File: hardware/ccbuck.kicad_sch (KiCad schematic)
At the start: 38 parts, among them J3 PWM/PFM, Q20 2N7002, U17 TPS552872RYQR

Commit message: craigenyah
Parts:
- renumbered C103 to C10, C104 to C11, C105 to C12, C106 to C13, C107 to C14, C88 to C15, C102 to C16, C124 to C17, C99 to C18, C100 to C19, C92 to C20, C91 to C21, C89 to C22, C90 to C23, C101 to C9, D10 to D9, J3 to J4, L2 to L1, Q20 to Q7, R126 to R18, R127 to R19, R125 to R20, R137 to R21, R138 to R22, R115 to R23, R114 to R24, R139 to R25, R41 to R26, R42 to R27, R132 to R28, R130 to R29, R131 to R30, TP35 to TP5, TP53 to TP6, TP51 to TP7, TP52 to TP8, U17 to U1

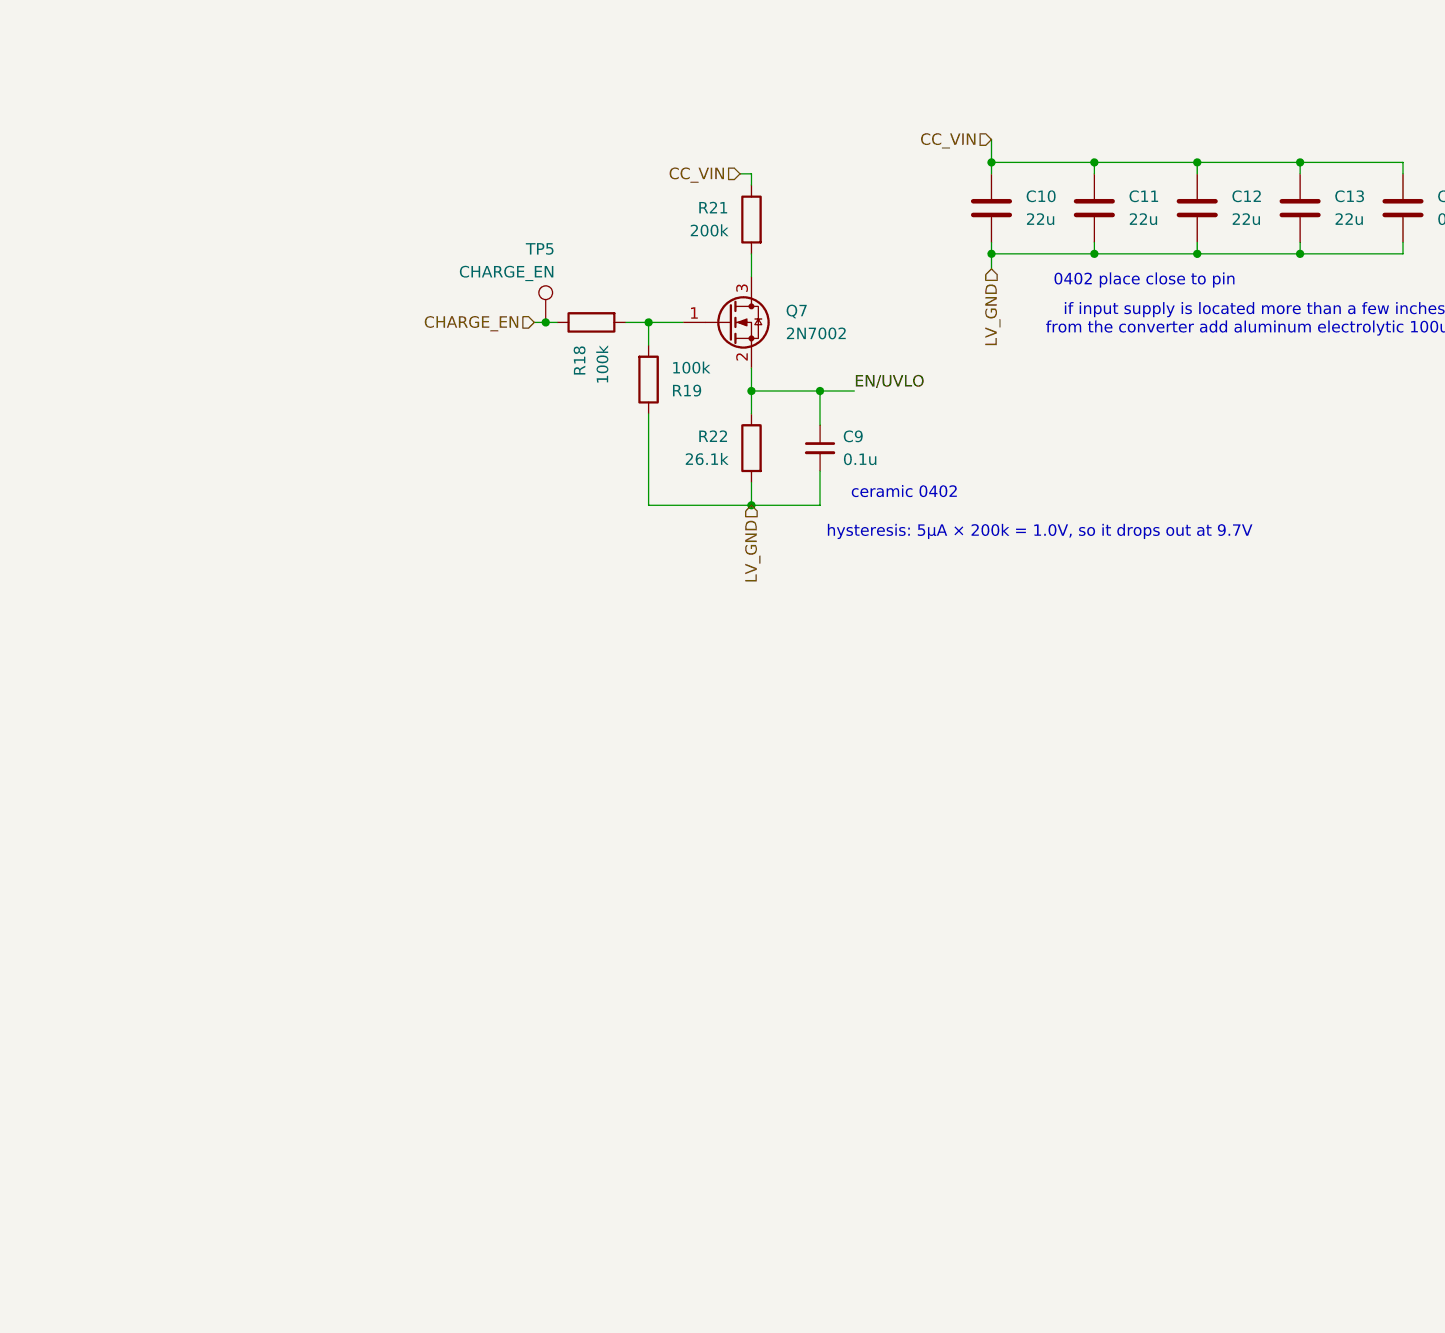
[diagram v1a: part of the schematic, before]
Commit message: switch to laptop
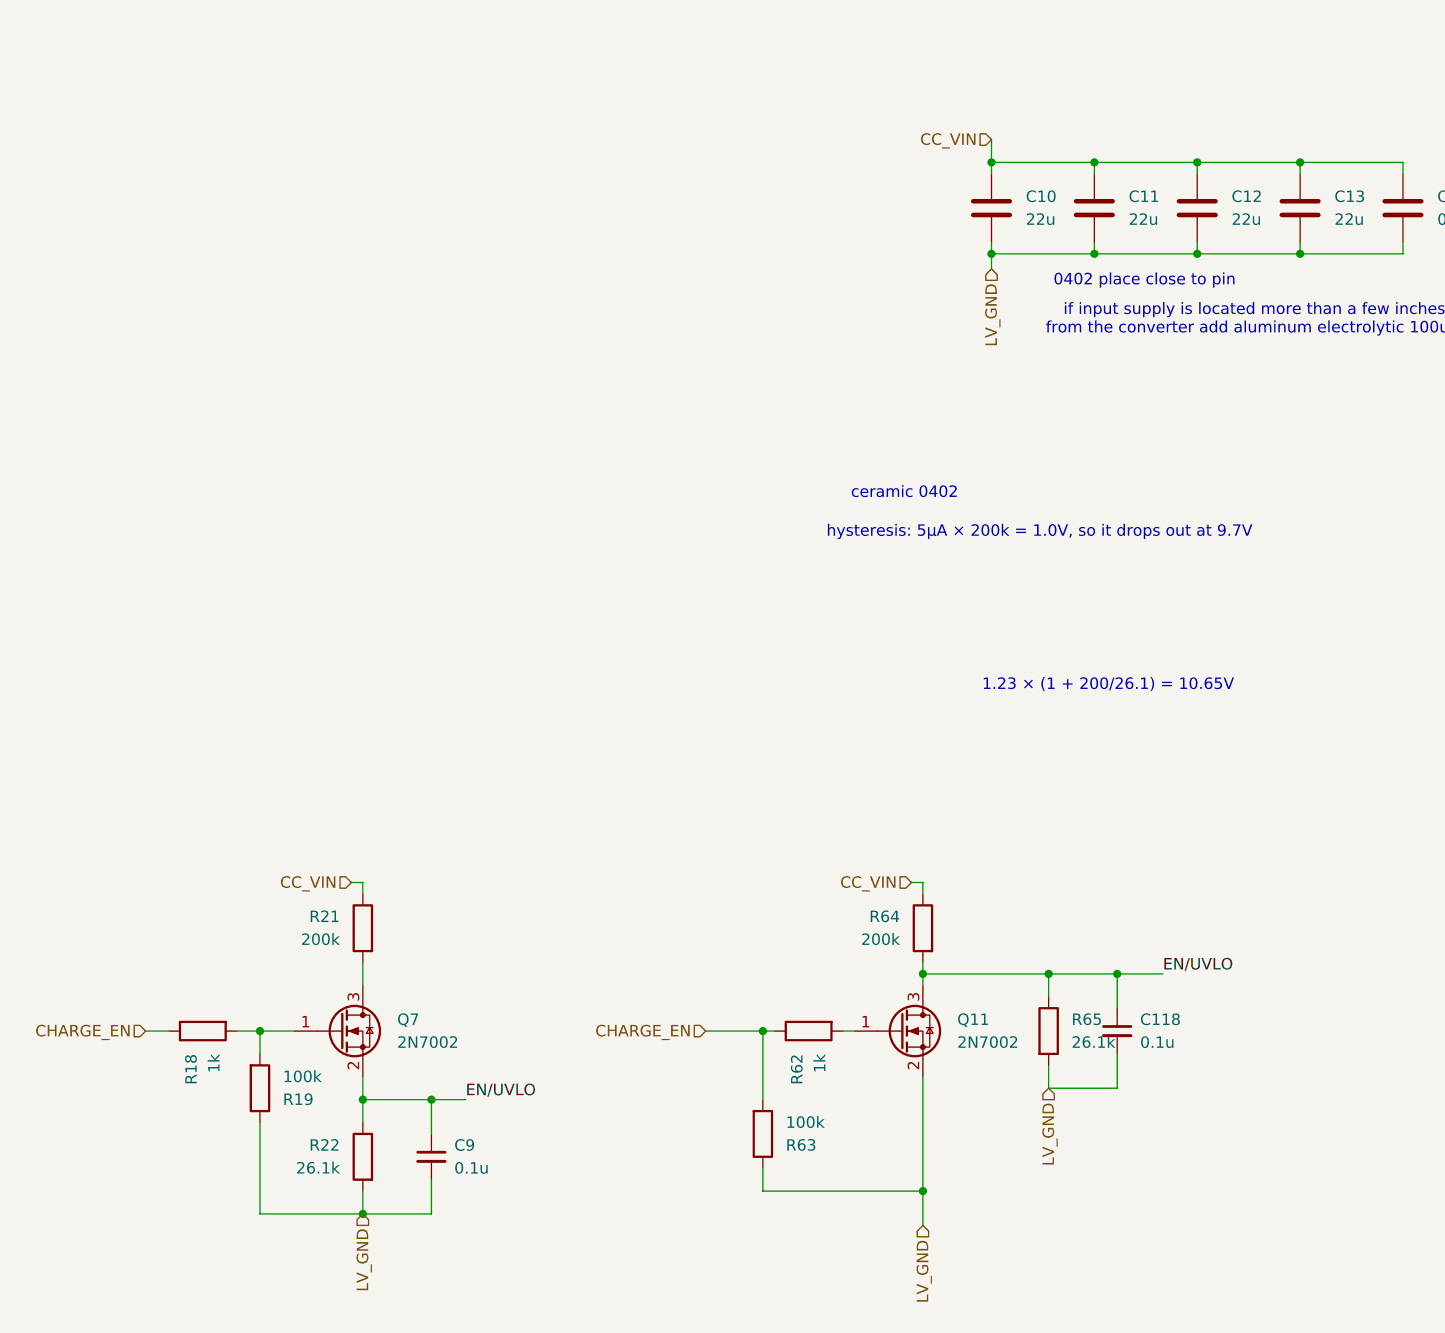
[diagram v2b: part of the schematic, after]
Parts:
- removed TP5: CHARGE_EN, TestPoint:TestPoint_Loop_D2.50mm_Drill1.0mm_LowProfile, symbol Connector:TestPoint
- added C118: 0.1u, Capacitor_SMD:C_0402_1005Metric_Pad0.74x0.62mm_HandSolder, symbol Device:C_Small
- added Q11: 2N7002, Package_TO_SOT_SMD:SOT-23, symbol Transistor_FET:2N7002
- added R62: 1k, Resistor_SMD:R_0603_1608Metric_Pad0.98x0.95mm_HandSolder, symbol Device:R
- added R63: 100k, Resistor_SMD:R_0603_1608Metric_Pad0.98x0.95mm_HandSolder, symbol Device:R
- added R64: 200k, Resistor_SMD:R_0603_1608Metric_Pad0.98x0.95mm_HandSolder, symbol Device:R
- added R65: 26.1k, Resistor_SMD:R_0603_1608Metric_Pad0.98x0.95mm_HandSolder, symbol Device:R
- R18: value 100k -> 1k
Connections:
- net CC_VIN: now also R64.1
- net CHARGE_EN: now also R62.1, R63.2
- net EN/UVLO: now also C118.1, Q11.3 (D), R64.2, R65.1
- net LV_GND: now also C118.2, Q11.2 (S), R63.1, R65.2
- new net: Q11.1 (G), R62.2
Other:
- note added: "1.23 × (1 + 200/26.1) = 10.65V"
- moved on the sheet: C9, Q7, R18, R19, R21, R22

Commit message: switch back to pc
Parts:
- removed C9: 0.1u, Capacitor_SMD:C_0402_1005Metric_Pad0.74x0.62mm_HandSolder, symbol Device:C_Small
- removed Q7: 2N7002, Package_TO_SOT_SMD:SOT-23, symbol Transistor_FET:2N7002
- removed R18: 1k, Resistor_SMD:R_0603_1608Metric_Pad0.98x0.95mm_HandSolder, symbol Device:R
- removed R19: 100k, Resistor_SMD:R_0603_1608Metric_Pad0.98x0.95mm_HandSolder, symbol Device:R
- removed R21: 200k, Resistor_SMD:R_0603_1608Metric_Pad0.98x0.95mm_HandSolder, symbol Device:R
- removed R22: 26.1k, Resistor_SMD:R_0603_1608Metric_Pad0.98x0.95mm_HandSolder, symbol Device:R
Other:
- moved on the sheet: C10, C11, C118, C12, C13, C14, Q11, R62, R63, R64, R65

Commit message: switch to pc...
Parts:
- R28: symbol Device:R_Shunt -> Device:R
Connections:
- net AGND is gone; now on net LV_GND: U1.17 (AGND)
- net SW1 is gone; now on net LV_GND: C18.2, L1.1, TP7.1, U1.8 (SW1)
- net CC_VOUT: now also U1.13 (ISN)
- net ISP: now also C20.1, C21.1, C22.1, C23.1, R28.2, U1.11 (VOUT); no longer R28.3
- removed net ISN: R28.2, U1.13 (ISN)
- removed net VOUT: C20.1, C21.1, C22.1, C23.1, R28.4, U1.11 (VOUT)
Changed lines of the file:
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@@
+	)
+	(junction
+		(at 187.96 109.22)
+		(diameter 0)
+		(color 0 0 0 0)
 	)
 	(junction
@@
 	)
 	(junction
+		(at 175.26 109.22)
+		(diameter 0)
+		(color 0 0 0 0)
+	)
+	(junction
 		(at 201.93 87.63)
 		(diameter 0)
@@
 	(wire
 		(pts
-			(xy 186.69 111.76) (xy 186.69 116.84)
-		)
-		(stroke
-			(width 0)
-			(type default)
-		)
-	)
-	(wire
-		(pts
 			(xy 81.28 161.29) (xy 81.28 157.48)
 		)
@@
 	(wire
 		(pts
+			(xy 187.96 109.22) (xy 198.12 109.22)
+		)
+		(stroke
+			(width 0)
+			(type default)
+		)
+	)
+	(wire
+		(pts
 			(xy 57.15 172.72) (xy 57.15 176.53)
 		)
@@
 	(wire
 		(pts
-			(xy 107.95 101.6) (xy 118.11 101.6)
-		)
-		(stroke
-			(width 0)
-			(type default)
-		)
-	)
-	(wire
-		(pts
 			(xy 238.76 128.27) (xy 248.92 128.27)
 		)
@@
 	(wire
 		(pts
-			(xy 175.26 104.14) (xy 166.37 104.14)
+			(xy 166.37 104.14) (xy 187.96 104.14)
 		)
 		(stroke
@@
 	(wire
 		(pts
-			(xy 189.23 109.22) (xy 198.12 109.22)
-		)
-		(stroke
-			(width 0)
-			(type default)
-		)
-	)
-	(wire
-		(pts
 			(xy 175.26 106.68) (xy 166.37 106.68)
 		)
@@
 	(wire
 		(pts
+			(xy 175.26 109.22) (xy 177.8 109.22)
+		)
+		(stroke
+			(width 0)
+			(type default)
+		)
+	)
+	(wire
+		(pts
 			(xy 107.95 86.36) (xy 118.11 86.36)
 		)
@@
 	(wire
 		(pts
+			(xy 185.42 109.22) (xy 187.96 109.22)
+		)
+		(stroke
+			(width 0)
+			(type default)
+		)
+	)
+	(wire
+		(pts
 			(xy 53.34 87.63) (xy 59.69 87.63)
 		)
@@
 	(wire
 		(pts
+			(xy 105.41 101.6) (xy 118.11 101.6)
+		)
+		(stroke
+			(width 0)
+			(type default)
+		)
+	)
+	(wire
+		(pts
 			(xy 90.17 120.65) (xy 78.74 120.65)
 		)
@@
 	(wire
 		(pts
-			(xy 175.26 93.98) (xy 166.37 93.98)
+			(xy 166.37 93.98) (xy 177.8 93.98)
 		)
 		(stroke
@@
 	(wire
 		(pts
+			(xy 187.96 104.14) (xy 187.96 109.22)
+		)
+		(stroke
+			(width 0)
+			(type default)
+		)
+	)
+	(wire
+		(pts
 			(xy 238.76 137.16) (xy 238.76 138.43)
 		)
@@
 	(wire
 		(pts
+			(xy 175.26 106.68) (xy 175.26 109.22)
+		)
+		(stroke
+			(width 0)
+			(type default)
+		)
+	)
+	(wire
+		(pts
 			(xy 198.12 133.35) (xy 198.12 132.08)
 		)
@@
 	(wire
 		(pts
-			(xy 181.61 111.76) (xy 181.61 116.84)
-		)
-		(stroke
-			(width 0)
-			(type default)
-		)
-	)
-	(wire
-		(pts
 			(xy 156.21 130.81) (xy 161.29 130.81)
 		)
@@
 	(wire
 		(pts
-			(xy 166.37 109.22) (xy 179.07 109.22)
+			(xy 166.37 109.22) (xy 175.26 109.22)
 		)
 		(stroke
@@
 		)
 	)
-	(label "ISN"
-		(at 186.69 116.84 180)
-		(effects
-			(font
-				(size 1.27 1.27)
-			)
-			(justify right bottom)
-		)
-	)
 	(label "FSW"
 		(at 57.15 43.18 180)
@@
 			)
 			(justify left bottom)
-		)
-	)
-	(label "ISP"
-		(at 181.61 116.84 180)
-		(effects
-			(font
-				(size 1.27 1.27)
-			)
-			(justify right bottom)
 		)
 	)
@@
 		(shape input)
 		(at 198.12 133.35 270)
+		(effects
+			(font
+				(size 1.27 1.27)
+			)
+			(justify right)
+		)
+	)
+	(hierarchical_label "LV_GND"
+		(shape input)
+		(at 177.8 93.98 270)
+		(effects
+			(font
+				(size 1.27 1.27)
+			)
+			(justify right)
+		)
+	)
+	(hierarchical_label "LV_GND"
+		(shape input)
+		(at 105.41 101.6 270)
 		(effects
 			(font
@@
 	)
 	(symbol
-		(lib_id "Device:R_Shunt")
-		(at 184.15 109.22 270)
+		(lib_id "Device:R")
+		(at 181.61 109.22 270)
 		(unit 1)
 		(body_style 1)
@@
 		(dnp no)
 		(property "Reference" "R28"
-			(at 184.15 102.87 90)
+			(at 181.61 102.87 90)
 			(show_name no)
 			(do_not_autoplace no)
@@
 		)
 		(property "Value" "25m"
-			(at 184.15 105.41 90)
+			(at 181.61 105.41 90)
 			(show_name no)
 			(do_not_autoplace no)
@@
 		)
 		(property "Footprint" "Resistor_SMD:R_2512_6332Metric_Pad1.40x3.35mm_HandSolder"
-			(at 184.15 107.442 90)
+			(at 181.61 107.442 90)
 			(hide yes)
 			(show_name no)
@@
 		)
 		(property "Datasheet" ""
-			(at 184.15 109.22 0)
-			(hide yes)
-			(show_name no)
-			(do_not_autoplace no)
-			(effects
-				(font
-					(size 1.27 1.27)
-				)
-			)
-		)
-		(property "Description" "Shunt resistor with Kelvin connections"
-			(at 184.15 109.22 0)
+			(at 181.61 109.22 0)
+			(hide yes)
+			(show_name no)
+			(do_not_autoplace no)
+			(effects
+				(font
+					(size 1.27 1.27)
+				)
+			)
+		)
+		(property "Description" "Resistor"
+			(at 181.61 109.22 0)
 			(hide yes)
 			(show_name no)
@@
 		)
 		(property "P/N" "1206W3F250MT5E"
-			(at 184.15 109.22 90)
+			(at 181.61 109.22 90)
 			(hide yes)
 			(show_name no)
@@
 		)
 		(property "LCSC P/N" "C105375"
-			(at 184.15 109.22 90)
+			(at 181.61 109.22 90)
 			(hide yes)
 			(show_name no)
@@
 		)
 		(property "LCSC" ""
-			(at 184.15 109.22 90)
+			(at 181.61 109.22 90)
 			(hide yes)
 			(show_name no)
@@
 		(pin "1"
 		)
-		(pin "3"
-		)
-		(pin "4"
-		)
 		(instances

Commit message: leaving apartment...
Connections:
- net ISP renamed VOUT
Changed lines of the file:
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@@
+	)
+	(junction
+		(at 175.26 109.22)
+		(diameter 0)
+		(color 0 0 0 0)
+	)
+	(junction
+		(at 201.93 87.63)
+		(diameter 0)
+		(color 0 0 0 0)
+	)
+	(junction
+		(at 57.15 172.72)
+		(diameter 0)
+		(color 0 0 0 0)
 	)
 	(junction
 		(at 161.29 130.81)
-		(diameter 0)
-		(color 0 0 0 0)
-	)
-	(junction
-		(at 175.26 109.22)
-		(diameter 0)
-		(color 0 0 0 0)
-	)
-	(junction
-		(at 201.93 87.63)
-		(diameter 0)
-		(color 0 0 0 0)
-	)
-	(junction
-		(at 57.15 172.72)
 		(diameter 0)
 		(color 0 0 0 0)
@@
 		)
 	)
-	(label "ISN"
-		(at 175.26 104.14 180)
-		(effects
-			(font
-				(size 1.27 1.27)
-			)
-			(justify right bottom)
-		)
-	)
 	(label "CHG_CC"
 		(at 124.46 44.45 0)
@@
 		)
 	)
-	(label "ISP"
-		(at 175.26 106.68 180)
-		(effects
-			(font
-				(size 1.27 1.27)
-			)
-			(justify right bottom)
-		)
-	)

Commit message: push
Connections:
- net PGND is gone; now on net LV_GND: U1.9 (PGND)
- net LV_GND: no longer C18.2, L1.1, TP7.1, U1.8 (SW1)
- new net SW1: C18.2, L1.1, TP7.1, U1.8 (SW1)
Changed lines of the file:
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@@
 	(wire
 		(pts
-			(xy 105.41 101.6) (xy 118.11 101.6)
+			(xy 107.95 101.6) (xy 118.11 101.6)
 		)
 		(stroke
@@
 	(wire
 		(pts
-			(xy 107.95 104.14) (xy 118.11 104.14)
+			(xy 105.41 104.14) (xy 118.11 104.14)
 		)
 		(stroke
@@
 	(hierarchical_label "LV_GND"
 		(shape input)
-		(at 105.41 101.6 270)
-		(effects
-			(font
+		(at 105.41 104.14 270)
+		(effects
+			(font

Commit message: oops
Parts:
- removed C118: 0.1u, Capacitor_SMD:C_0402_1005Metric_Pad0.74x0.62mm_HandSolder, symbol Device:C_Small
- removed Q11: 2N7002, Package_TO_SOT_SMD:SOT-23, symbol Transistor_FET:2N7002
- removed R62: 1k, Resistor_SMD:R_0603_1608Metric_Pad0.98x0.95mm_HandSolder, symbol Device:R
- removed R63: 100k, Resistor_SMD:R_0603_1608Metric_Pad0.98x0.95mm_HandSolder, symbol Device:R
- removed R64: 200k, Resistor_SMD:R_0603_1608Metric_Pad0.98x0.95mm_HandSolder, symbol Device:R
- removed R65: 26.1k, Resistor_SMD:R_0603_1608Metric_Pad0.98x0.95mm_HandSolder, symbol Device:R
- added C119: 0.1u, Capacitor_SMD:C_0603_1608Metric_Pad1.08x0.95mm_HandSolder, symbol Device:C_Small
- added Q1: BSS84, Package_TO_SOT_SMD:SOT-23, symbol Transistor_FET:BSS84
- added Q22: 2N7002, Package_TO_SOT_SMD:SOT-23, symbol Transistor_FET:2N7002
- added R148: 200k, Resistor_SMD:R_0603_1608Metric_Pad0.98x0.95mm_HandSolder, symbol Device:R
- added R149: 26.1k, Resistor_SMD:R_0603_1608Metric_Pad0.98x0.95mm_HandSolder, symbol Device:R
- added R155, R157: 100k, Resistor_SMD:R_0603_1608Metric_Pad0.98x0.95mm_HandSolder, symbol Device:R
- added R156: 1k, Resistor_SMD:R_0603_1608Metric_Pad0.98x0.95mm_HandSolder, symbol Device:R
- C10, C11, C12, C13, C20, C21, C22, C23: P/N (none) -> MLASU168SB5105KTNA01
- C14: footprint Capacitor_SMD:C_0402_1005Metric_Pad0.74x0.62mm_HandSolder -> Capacitor_SMD:C_0603_1608Metric_Pad1.08x0.95mm_HandSolder; LCSC P/N (none) -> C14663; P/N (none) -> MLASH168SB7104KTNA01
- C15: LCSC P/N (none) -> C57112; P/N (none) -> MSASH168SB5103KTNA01
- C16: P/N (none) -> 06035C472K4T2A
- C17: LCSC P/N C22387800 -> C6962403; P/N (none) -> 08055D475KAT4A
- C18, C19: P/N (none) -> MLASH168SB7104KTNA01
- U1: LCSC P/N (none) -> C22427496; P/N (none) -> TPS552872RYQR
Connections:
- net CC_VIN: now also Q1.2 (S), R155.1
- net CHARGE_EN: now also R156.1, R157.2
- net EN/UVLO: now also C119.1, R148.2, R149.1
- net LV_GND: now also C119.2, Q22.2 (S), R149.2, R157.1
- new net: Q1.1 (G), Q22.3 (D), R155.2
- new net: Q1.3 (D), R148.1
- new net: Q22.1 (G), R156.2

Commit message: added most p/n, still in progress but saving
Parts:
- D8, D9: LCSC P/N (none) -> -- mixed values --; P/N (none) -> -- mixed values --
- R148: P/N (none) -> 0603WAF2003T5E
- R155: Assemble (none) -> -- mixed values --; LCSC P/N C25811 -> C25803; P/N (none) -> CRCW0603100KFKEE
- R156: Assemble (none) -> -- mixed values --; LCSC P/N (none) -> C21190; P/N (none) -> CRCW06031K00FKEI
- R157, R23, R24, R29: Assemble (none) -> -- mixed values --; LCSC P/N (none) -> C25803; P/N (none) -> CRCW0603100KFKEE
- R20: LCSC P/N (none) -> C177599; P/N (none) -> RCT0349K9FLF
- R25: LCSC P/N (none) -> C177300; P/N (none) -> RCT0330KJLF
- R26, R27: LCSC P/N (none) -> C177867; P/N (none) -> RCT031K3FLF
- R30: LCSC P/N (none) -> C177496; P/N (none) -> RCT038K66FLF
